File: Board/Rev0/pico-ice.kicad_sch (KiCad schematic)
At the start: 98 parts, among them J2 PMOD_BANK0, J5 PMOD_BANK0_1, J6 PMOD_BANK2, J7 SPARES, SW1 Boot, SW2 SW_Push, U2 W25Q32JVSSIM, U5 APS6404L-3SQN

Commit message: Fixed PMOD connections and other major changes. Needs detailed review.
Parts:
- removed C36, C37: 0.1u, Capacitor_SMD:C_0603_1608Metric, symbol UPduino_v3.0:Device_C
- removed J5: PMOD_BANK0_1, symbol Connector_Generic:Conn_02x06_Row_Letter_First
- removed SW1: Boot, symbol Switch:SW_Push
- added J5: Conn_ARM_JTAG_SWD_10, symbol Connector:Conn_ARM_JTAG_SWD_10
- added J8: Dual PMOD B, symbol Connector_Generic:Conn_02x06_Row_Letter_First
- added J?: Conn_01x02, symbol Connector_Generic:Conn_01x02
- added PTC1: MF-FSMF035X-2, Resistor_SMD:R_0603_1608Metric, symbol UPduino_v3.0:Device_R
- added R21: 10K, Resistor_SMD:R_0603_1608Metric, symbol UPduino_v3.0:Device_R
- added SW?: Boot, symbol Switch:SW_Push
- J2: value PMOD_BANK0 -> SPARE
- J4: value (none) -> Dual PMOD A
- J6: value PMOD_BANK2 -> Single PMOD
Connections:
- net +3V3: now also R16.2, SW2.1, J5.1 (VTref), J8.a6 (Pin_a6), J8.b6 (Pin_b6); no longer J2.a6 (Pin_a6), J2.b6 (Pin_b6), R16.1
- net GND: now also J5.3 (GND), J5.5 (GND), J5.9 (GNDDetect), J8.a5 (Pin_a5), J8.b5 (Pin_b5), J?.2 (Pin_2), R21.2, SW?.1; no longer J2.a5 (Pin_a5), J7.a5 (Pin_a5)
- net GPIO26_ADC0: now also J2.a3 (Pin_a3); no longer J3.a4 (Pin_a4)
- net GPIO27_ADC1: now also J2.a2 (Pin_a2); no longer J3.a3 (Pin_a3)
- net GPIO28_ADC2: now also J2.a1 (Pin_a1); no longer J3.a2 (Pin_a2)
- net ICE_11: now also J2.a6 (Pin_a6), U3.11 (GPIO8); no longer J6.a4 (Pin_a4), U3.7 (GPIO5)
- net ICE_20_G3: no longer U3.4 (GPIO2)
- net ICE_21: now also J6.a3 (Pin_a3), U3.6 (GPIO4); no longer J6.b2 (Pin_b2), U3.9 (GPIO7)
- net ICE_23: now also J6.b2 (Pin_b2); no longer J2.a2 (Pin_a2)
- net ICE_25: now also J6.a2 (Pin_a2), U3.5 (GPIO3); no longer J2.a1 (Pin_a1)
- net ICE_26: now also J6.b1 (Pin_b1); no longer J2.a4 (Pin_a4)
- net ICE_27: now also J6.a1 (Pin_a1), U3.3 (GPIO1); no longer J2.a3 (Pin_a3)
- net ICE_28: now also J8.b4 (Pin_b4); no longer J2.b1 (Pin_b1)
- net ICE_31: now also J8.a4 (Pin_a4); no longer J2.b2 (Pin_b2)
- net ICE_32: now also J8.b3 (Pin_b3); no longer J2.b3 (Pin_b3)
- net ICE_34: now also J8.a3 (Pin_a3); no longer J2.b4 (Pin_b4)
- net ICE_35_G0: now also J2.b4 (Pin_b4)
- net ICE_36: now also J8.b2 (Pin_b2)
- net ICE_38: now also J8.a2 (Pin_a2)
- net ICE_42: now also J8.b1 (Pin_b1)
- net ICE_43: now also J8.a1 (Pin_a1)
- net ICE_6: now also J2.b1 (Pin_b1), U3.7 (GPIO5); no longer J6.a1 (Pin_a1), U3.3 (GPIO1)
- net ICE_9: now also J2.b2 (Pin_b2), U3.8 (GPIO6); no longer J6.a2 (Pin_a2), U3.5 (GPIO3)
- net ICE_DONE: now also J7.b6 (Pin_b6)
- net ICE_FLASH_IO2: now also U6.12 (IOB_22a); no longer U6.19 (IOB_29b)
- net ICE_FLASH_IO3: now also U6.13 (IOB_24a); no longer U6.18 (IOB_31b)
- net ICE_LED_B: now also J7.b4 (Pin_b4), U6.40 (RGB1)
- net ICE_LED_G: now also J7.b3 (Pin_b3), U6.39 (RGB0)
- net ICE_LED_R: now also J7.b5 (Pin_b5), U6.41 (RGB2)
- net ICE_SCK: now also J7.a4 (Pin_a4); no longer J7.b5 (Pin_b5)
- net ICE_SI: now also J7.a3 (Pin_a3); no longer J7.b4 (Pin_b4)
- net ICE_SO: now also J7.a2 (Pin_a2); no longer J7.b3 (Pin_b3)
- net ICE_SSN: now also J7.a1 (Pin_a1); no longer J7.b6 (Pin_b6)
- net PICO_LED_B: now also U3.41 (GPIO29_ADC3)
- net PICO_LED_G: now also U3.17 (GPIO14)
- net PICO_LED_R: now also U3.16 (GPIO13)
- net SRAM_SSN: now also J2.a4 (Pin_a4)
- net SWCLK: now also J5.4 (SWDCLK/TCK)
- net SWD: now also J5.2 (SWDIO/TMS)
- net VBUS: now also J2.b6 (Pin_b6), PTC1.1; no longer J1.1 (VBUS)
- net ~{USB_BOOT}: now also J?.1 (Pin_1)
- net PICO_9_SS1n: now reaches U3.12 (GPIO9)
- net PICO_9_SS1n: now also J3.a1 (Pin_a1)
- net PICO_10_SCK1: now reaches U3.13 (GPIO10)
- net PICO_10_SCK1: now also J3.a4 (Pin_a4)
- net PICO_11_MOSI1: now reaches U3.14 (GPIO11)
- net PICO_11_MOSI1: now also J3.a2 (Pin_a2)
- net PICO_12_MISO1: now reaches U3.15 (GPIO12)
- net PICO_12_MISO1: now also J3.a3 (Pin_a3)
- removed net GPIO29_ADC3: J3.a1 (Pin_a1), U3.41 (GPIO29_ADC3)
- net ICE_0A renamed ICE_3
- net ICE_3: now also U6.3 (IOB_9b); no longer U6.46 (IOB_0a)
- removed net ICE_10: J6.a3 (Pin_a3), U3.6 (GPIO4), U6.10 (IOB_18a)
- removed net ICE_12: J6.b1 (Pin_b1), U3.8 (GPIO6), U6.12 (IOB_22a)
- removed net ICE_13_PB: J6.b3 (Pin_b3), SW2.2, U3.11 (GPIO8), U6.13 (IOB_24a)
- net ICE_2A renamed ICE_46
- net ICE_46: now also U6.46 (IOB_0a); no longer U6.47 (IOB_2a)
- net ICE_3B_G6 renamed ICE_44_G6
- net ICE_4A renamed ICE_48
- net ICE_5B renamed ICE_45
- net ICE_6A renamed ICE_2
- net ICE_2: now also J4.a2 (Pin_a2); no longer J4.a3 (Pin_a3)
- net ICE_8A renamed ICE_4
- net ICE_4: now also J4.a1 (Pin_a1); no longer J4.a2 (Pin_a2)
- removed net ICE_9B: J4.a1 (Pin_a1), U6.3 (IOB_9b)
- net ICE_RST_N renamed ICE_RSTn
- net ICE_RSTn: now also J7.a5 (Pin_a5)
- removed net LED_B: J7.a2 (Pin_a2), U6.40 (RGB1)
- removed net LED_G: J7.a1 (Pin_a1), U6.39 (RGB0)
- removed net LED_R: J7.a3 (Pin_a3), U6.41 (RGB2)
- net PICO_22 renamed PICO_22_SCK0
- net PICO_22_SCK0: now also J3.b4 (Pin_b4); no longer J3.b1 (Pin_b1)
- net PICO_23 renamed PICO_23_MOSI0
- net PICO_24 renamed PICO_24_MISO0
- net PICO_25 renamed PICO_25_SSn0
- net PICO_25_SSn0: now also J3.b1 (Pin_b1); no longer J3.b4 (Pin_b4)
- net RUN renamed RESETn
- net RESETn: now also J5.10 (~{RESET}), SW?.2
- new net: J1.1 (VBUS), PTC1.2
- new net ICE_10_PB: R21.1, SW2.2
- new net ICE_10|PB: J2.b3 (Pin_b3), U3.9 (GPIO7), U6.10 (IOB_18a)
- new net ICE_18: J6.b3 (Pin_b3), U6.18 (IOB_31b)
- new net ICE_19: J6.a4 (Pin_a4), U3.4 (GPIO2), U6.19 (IOB_29b)
- new net ICE_47: J4.a3 (Pin_a3), U6.47 (IOB_2a)
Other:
- note added: "Dual iCE PMOD"
- note added: "Layout Note: Separate PMOD's by 0.9" (center-center)"
- note added: "PICO PMOD A"
- note added: "PICO PMOD B"
- note added: "PICO SWD, Boot"
- note added: "Pico PMOD"
- note added: "Pico-FPGA Bus"
- note added: "Rx"
- note added: "SCK"
- note added: "SSn"
- note added: "TODO: - How about the RUN, SWD and SWCLK pins? How can we put those in an easily accessible spot for the user? - Unify parts to minimize BoM"
- note added: "Tx"
- note added: "iCE PMOD"
- note removed: "Change to standard SPI config of PMOD"
- note removed: "Dedicated Pico-FPGA Bus"
- note removed: "PICO SWD"
- note removed: "Should we add reset and 3.3V/Ground as well to a standard 10 pin SWD?"
- note removed: "TODO: - Make pinout of PMOD's same as the iCEBreaker - Add a port for the VIO for Bank 2 - How about the RUN, SWD and SWCLK pins? How can we put those in an easily accessible spot for the user? - Unify parts to minimize BoM - Check on diff pairs to PMOD's being placed close to each other"
- moved on the sheet: C14, C20, C26, C38, C39, C40, C41, C8, FID1, FID2, FID3, FID4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

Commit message: Moved files for review to Review, reallocated pinlist on RP
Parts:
- C1, C2: value (none) -> 27p; footprint (none) -> Capacitor_SMD:C_0402_1005Metric
- C11, C6: value (none) -> 1u; footprint (none) -> Capacitor_SMD:C_0402_1005Metric
- C13, C22, C25, C30, C31, C32, C34, C9: value (none) -> 4.7u; footprint (none) -> Capacitor_SMD:C_0603_1608Metric
- C14, C21, C24, C26, C27, C28, C29, C33: value (none) -> 0.1u; footprint (none) -> Capacitor_SMD:C_0603_1608Metric
- D1: value (none) -> 1N4148WT-7; footprint (none) -> Diode_SMD:D_SOD-523
- D2: value (none) -> CLMVC-FKA-CLBDGL7LBB79353; footprint (none) -> VS.preety:LED_Cree-PLCC4_2x2mm_CW
- D3: value (none) -> LTST-C191KGKT; footprint (none) -> LED_SMD:LED_0603_1608Metric
- FID1, FID2, FID3, FID4, FID5, FID6: value (none) -> Fiducial; footprint (none) -> Fiducial:Fiducial_0.75mm_Mask1.5mm
- H1, H2, H3, H4: value (none) -> MountingHole; footprint (none) -> MountingHole:MountingHole_2.7mm_M2.5
- J1: value (none) -> Connector_USB_B_Micro
- J3: value (none) -> PMOD_PICO
- J?: value Conn_01x02 -> BOOT_SEL
- R1, R2: value (none) -> 1k; footprint (none) -> Capacitor_SMD:C_0402_1005Metric
- R10, SJ4, SJ5: value (none) -> SHORT; footprint (none) -> vs:ShortedJumper-2_P1.3mm_Bridged_Pad1.0x1.0mm
- R11: value (none) -> 100; footprint (none) -> Resistor_SMD:R_0603_1608Metric
- R12, R13, R7, R8, R9: value (none) -> 10K; footprint (none) -> Resistor_SMD:R_0603_1608Metric
- R14: value (none) -> 2.2K; footprint (none) -> Resistor_SMD:R_0603_1608Metric
- R4, R5: value (none) -> 27; footprint (none) -> Capacitor_SMD:C_0402_1005Metric
- SJ6: value (none) -> OPEN; footprint (none) -> vs:SolderJumper-2_0603_Open_TrianglePad1.0x1.5mm
- SW?: value Boot -> ~{RESET}
- TP1: value (none) -> TestPoint; footprint (none) -> TestPoint:TestPoint_Pad_D1.0mm
- U1: value (none) -> NCP1117-3.3_SOT223; footprint (none) -> Package_TO_SOT_SMD:SOT-223-3_TabPin2
- U3: value (none) -> RP2040; footprint (none) -> RP2040_minimal:RP2040-QFN-56
- U4: value (none) -> AP2127K-1.2; footprint (none) -> vs:SOT-23-5
- U6: value (none) -> ICE40UP5K-SG48ITR; footprint (none) -> Package_DFN_QFN:QFN-48-1EP_7x7mm_P0.5mm_EP5.6x5.6mm
- U8: value (none) -> W25Q32JVSSIM; footprint (none) -> Package_SO:SOIC-8_5.23x5.23mm_P1.27mm
- Y1: value (none) -> ABLS-12.000MHZ-B4-T; footprint (none) -> RP2040_minimal:Crystal_SMD_HC49-US
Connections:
- net ICE_10_PB is gone; now on net ICE_10|PB: R21.1, SW2.2
- net RESETn is gone; now on net ~{RESET}: J5.10 (~{RESET}), SW?.2, U3.26 (RUN)
- net ICE_10|PB: no longer U3.9 (GPIO7)
- net ICE_11: no longer U3.11 (GPIO8)
- net ICE_18: now also U3.14 (GPIO11)
- net ICE_19: now also U3.9 (GPIO7); no longer U3.4 (GPIO2)
- net ICE_20_G3: now also U3.13 (GPIO10)
- net ICE_21: now also U3.8 (GPIO6); no longer U3.6 (GPIO4)
- net ICE_23: now also U3.12 (GPIO9)
- net ICE_25: now also U3.7 (GPIO5); no longer U3.5 (GPIO3)
- net ICE_26: now also U3.11 (GPIO8)
- net ICE_27: now also U3.6 (GPIO4); no longer U3.3 (GPIO1)
- net ICE_6: no longer U3.7 (GPIO5)
- net ICE_9: no longer U3.8 (GPIO6)
- net ICE_CLK: now also U3.32 (GPIO21); no longer U3.2 (GPIO0)
- net ICE_DONE: now also U3.38 (GPIO26_ADC0); no longer U3.32 (GPIO21)
- net ICE_RSTn: now also U3.37 (GPIO25); no longer U3.31 (GPIO20)
- net ICE_SCK: now also U3.4 (GPIO2); no longer U3.29 (GPIO18)
- net ICE_SI: now also U3.5 (GPIO3); no longer U3.30 (GPIO19)
- net ICE_SO: now also U3.2 (GPIO0); no longer U3.27 (GPIO16)
- net ICE_SSN: now also U3.3 (GPIO1); no longer U3.28 (GPIO17)
- net PICO_LED_B: now also U3.36 (GPIO24); no longer U3.41 (GPIO29_ADC3)
- net PICO_LED_G: now also U3.35 (GPIO23); no longer U3.17 (GPIO14)
- net PICO_LED_R: now also U3.34 (GPIO22); no longer U3.16 (GPIO13)
- net SRAM_SSN: now also U3.31 (GPIO20); no longer U3.18 (GPIO15)
- net ~{RESET}: now reaches R16.1
- net GPIO26_ADC0 renamed ADC3
- net ADC3: now also U3.41 (GPIO29_ADC3); no longer U3.38 (GPIO26_ADC0)
- net GPIO27_ADC1 renamed ADC1
- net ADC1: now also J2.a1 (Pin_a1); no longer J2.a2 (Pin_a2)
- net GPIO28_ADC2 renamed ADC2
- net ADC2: now also J2.a2 (Pin_a2); no longer J2.a1 (Pin_a1)
- net PICO_10_SCK1 renamed PICO_PMOD_A4
- net PICO_PMOD_A4: now also U3.18 (GPIO15); no longer U3.13 (GPIO10)
- net PICO_11_MOSI1 renamed PICO_PMOD_A2
- net PICO_PMOD_A2: now also U3.16 (GPIO13); no longer U3.14 (GPIO11)
- net PICO_12_MISO1 renamed PICO_PMOD_A1
- net PICO_PMOD_A1: now also J3.a1 (Pin_a1); no longer J3.a3 (Pin_a3)
- net PICO_22_SCK0 renamed PICO_PMOD_B4
- net PICO_PMOD_B4: now also U3.30 (GPIO19); no longer U3.34 (GPIO22)
- net PICO_23_MOSI0 renamed PICO_PMOD_B2
- net PICO_PMOD_B2: now also U3.28 (GPIO17); no longer U3.35 (GPIO23)
- net PICO_24_MISO0 renamed PICO_PMOD_B3
- net PICO_PMOD_B3: now also U3.29 (GPIO18); no longer U3.36 (GPIO24)
- net PICO_25_SSn0 renamed PICO_PMOD_B1
- net PICO_PMOD_B1: now also U3.27 (GPIO16); no longer U3.37 (GPIO25)
- removed net PICO_9_SS1n: J3.a1 (Pin_a1), U3.12 (GPIO9)
- new net PICO_PMOD_A3: J3.a3 (Pin_a3), U3.17 (GPIO14)
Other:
- note added: "PICO SWD, Reset"
- note removed: "PICO PMOD A"
- note removed: "PICO PMOD B"
- note removed: "PICO SWD, Boot"
- title: PICOICe -> PICO-iCE
- moved on the sheet: R6

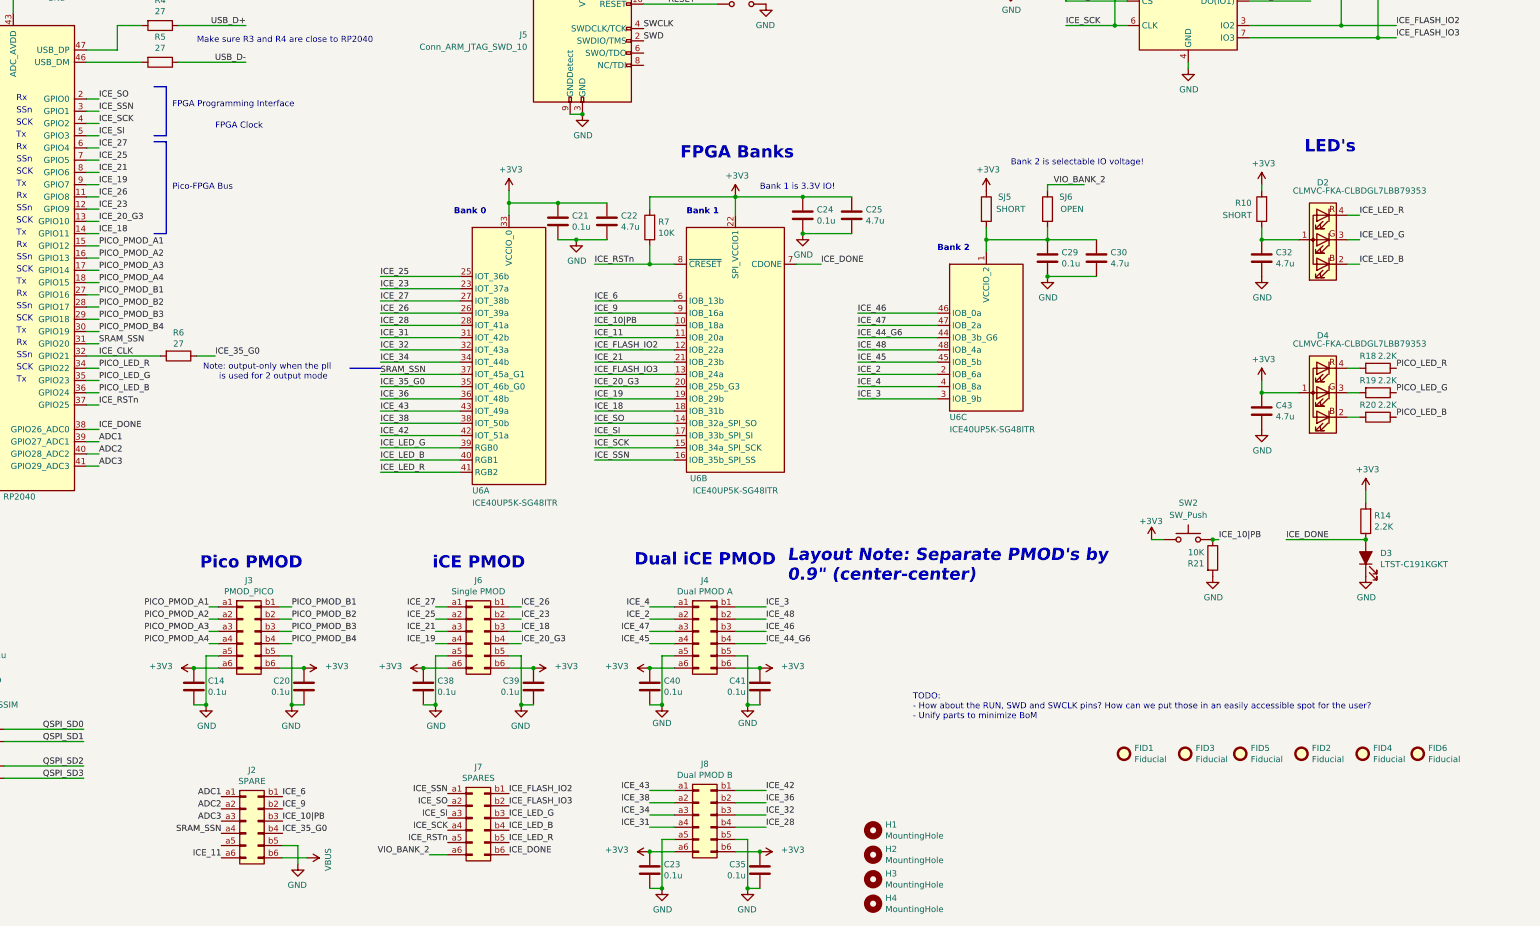
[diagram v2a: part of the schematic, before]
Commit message: Added external clock from RP to external header
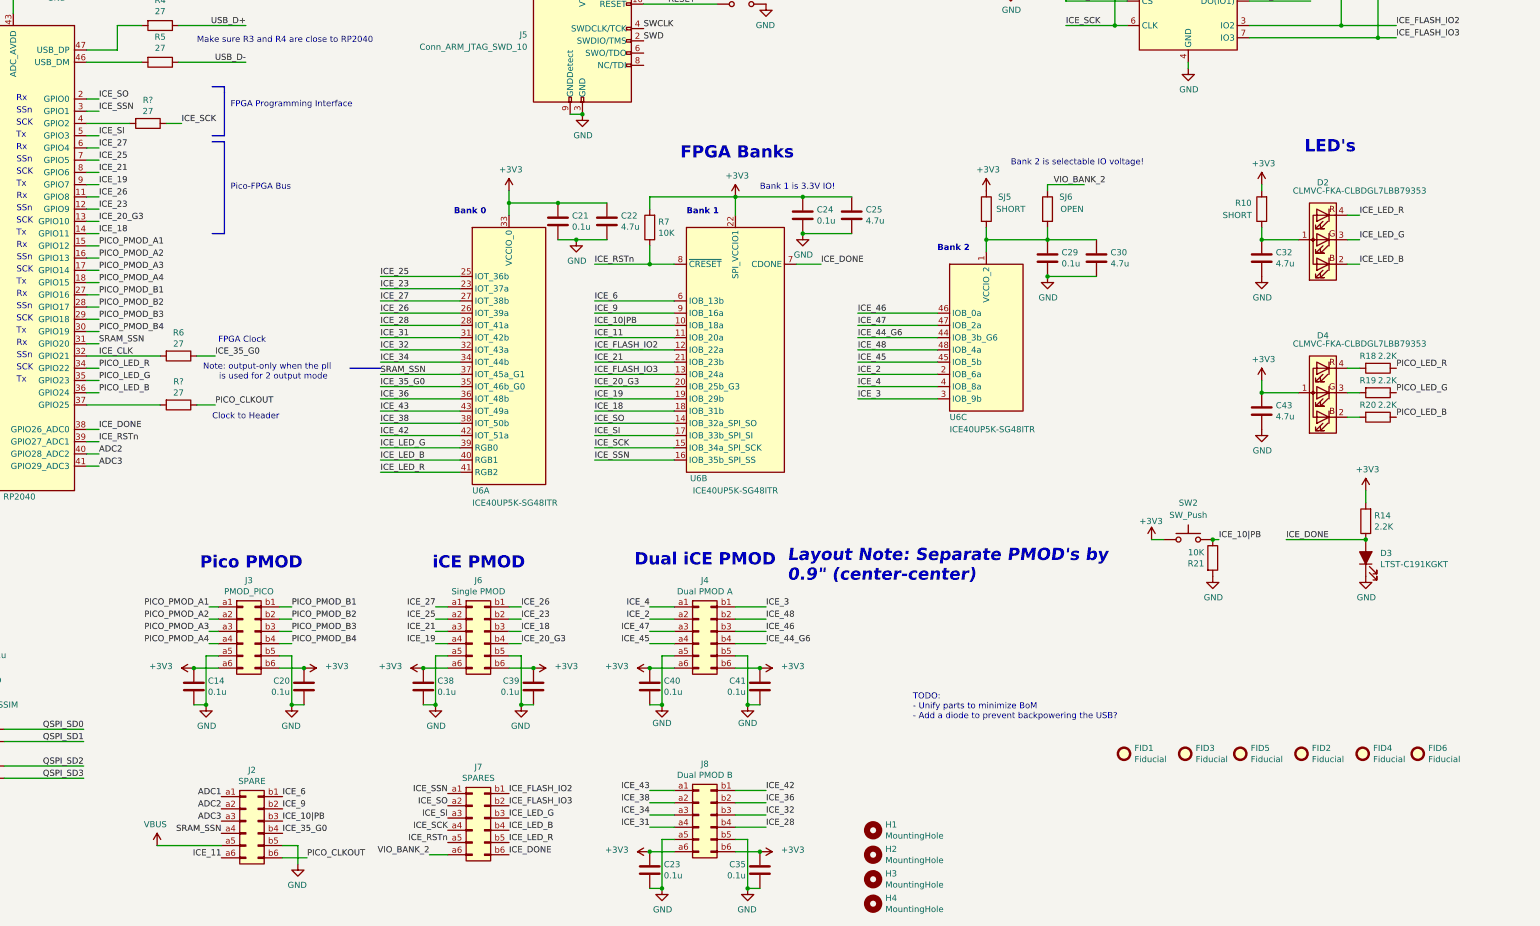
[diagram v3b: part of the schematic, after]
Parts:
- added R? (x2): 27, Capacitor_SMD:C_0402_1005Metric, symbol Device:R
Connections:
- net ADC1: no longer U3.39 (GPIO27_ADC1)
- net ICE_RSTn: now also U3.39 (GPIO27_ADC1); no longer U3.37 (GPIO25)
- net ICE_SCK: now also R?.1; no longer U3.4 (GPIO2)
- net VBUS: now also J2.a5 (Pin_a5); no longer J2.b6 (Pin_b6)
- new net: R?.2, U3.37 (GPIO25)
- new net: R?.2, U3.4 (GPIO2)
- new net PICO_CLKOUT: J2.b6 (Pin_b6), R?.1
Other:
- note added: "Clock to Header"
- note added: "TODO: - Unify parts to minimize BoM - Add a diode to prevent backpowering the USB?"
- note removed: "TODO: - How about the RUN, SWD and SWCLK pins? How can we put those in an easily accessible spot for the user? - Unify parts to minimize BoM"

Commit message: Added MPN's for a few parts
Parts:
- D2, D4: value CLMVC-FKA-CLBDGL7LBB79353 -> MHPA1010RGBDT
- U1: value NCP1117-3.3_SOT223 -> NCP1117ST33T3G
- U2, U8: value W25Q32JVSSIM -> W25Q32JVSSIQ
- gave numbers to parts that had none: 4
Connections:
- net +3V3: now also C28.1, D1.2 (A)
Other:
- moved on the sheet: C13, C3, C7, C9, PTC1, TP1, U1, U4
